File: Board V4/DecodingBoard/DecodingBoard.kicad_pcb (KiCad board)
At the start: 4 copper layers, 47.5 x 41 mm, 71 parts, among them IC1 STM32WBA65CIU6, IC2 RN4871-V_RM140, IC3 MCP111-195I_TO, J1 UJ20-C-H-G-SMT-1-P16-TR, J3 TSM-106-02-T-SH-LC, J4 2053380002, J5 5037630491, J6 5040500691, SW1 TL3305BF100QG, SW2 TL3305BF100QG, U1 ESDS302DBVR, U2 TPS7A7200RGWT, U3 USBLC6-2SC6, U4 TPS2121RUXR

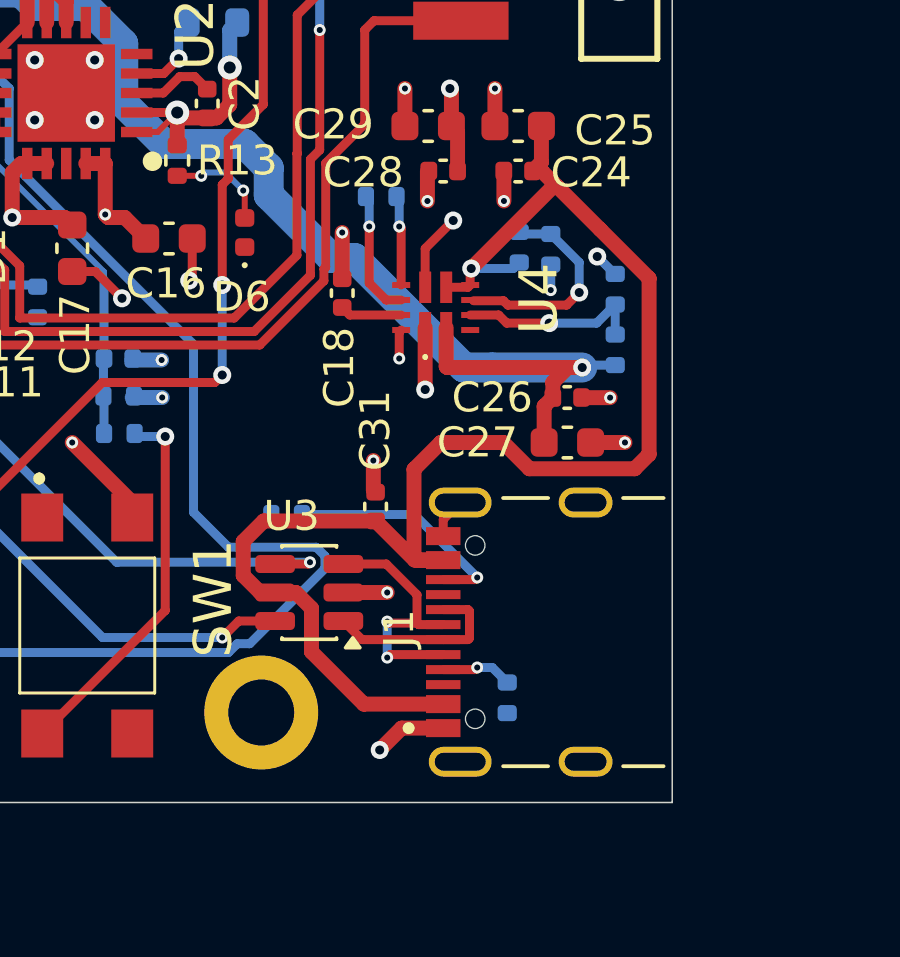
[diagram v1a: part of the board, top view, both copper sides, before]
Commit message: Changed layout for new USB-C connector
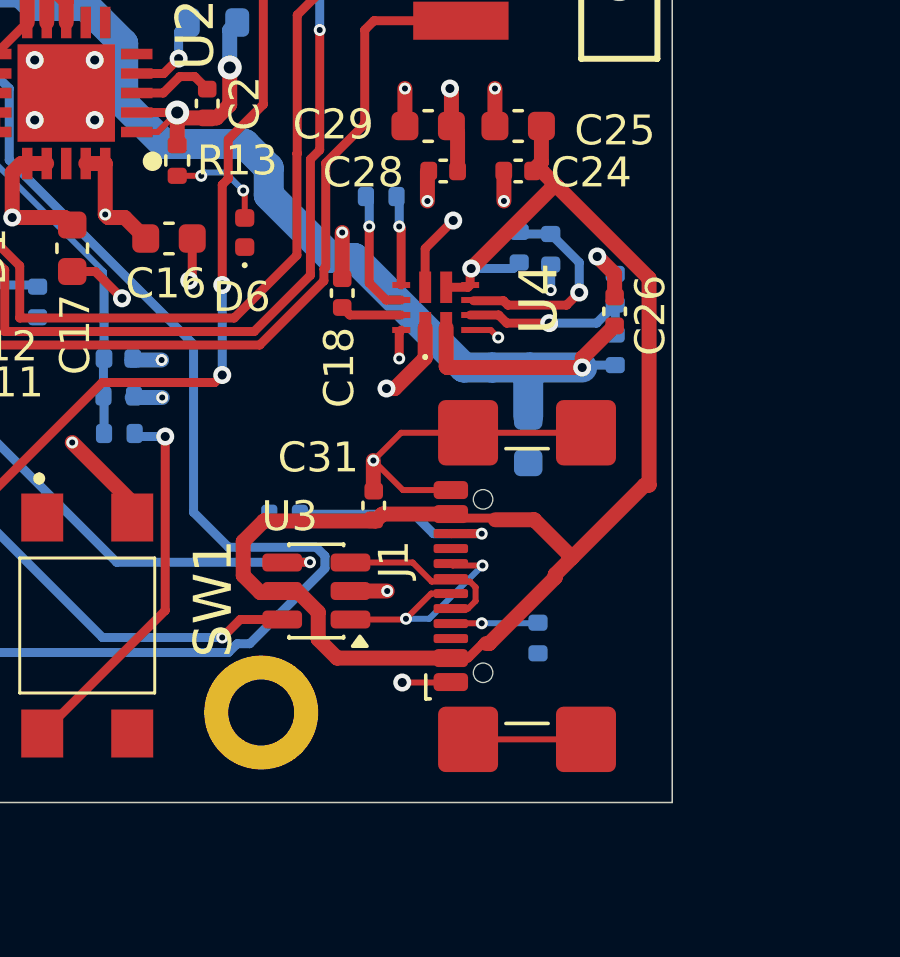
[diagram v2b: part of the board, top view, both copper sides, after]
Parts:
- C27: moved to B.Cu
- J1: value UJ20-C-H-G-SMT-1-P16-TR -> USB_C_Receptacle_USB2.0_16P; footprint Footprints:SAMESKY_UJ20-C-H-G-SMT-1-P16-TR -> Connector_USB:USB_C_Receptacle_GCT_USB4110
- moved J1 3.74 mm to (140.8, 82.8)
- moved C26 3.28 mm to (142.6, 73.6), turned to 90 degrees
- moved R5 2.24 mm to (140.0, 84.5)
- moved C27 1.31 mm to (139.7, 77.9), turned to -90 degrees
- moved U3 0.24 mm to (132.6, 83.0)
- moved C31 0.07 mm to (134.6, 80.1)
- moved R6 0.07 mm to (131.6, 80.4)
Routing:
- net GND: track 81.5 -> 94.6 mm, vias 53 -> 52
- net /USB-C circuit/USB_D-: track 8.84 -> 5.90 mm, vias 2 -> 0
- net /USB-C circuit/USB_D+: track 6.28 -> 8.07 mm, vias 0 -> 2
- net /Power switching and voltage adaptation/from USB-C: track 50.6 -> 52.2 mm
- net +5V: track 22.4 -> 23.0 mm
- net /Power: track 54.8 -> 55.4 mm
- net /USB-C circuit/USB_CC1: track 2.37 -> 2.92 mm
- net /USB-C circuit/USB_CC2: track 7.87 -> 7.36 mm

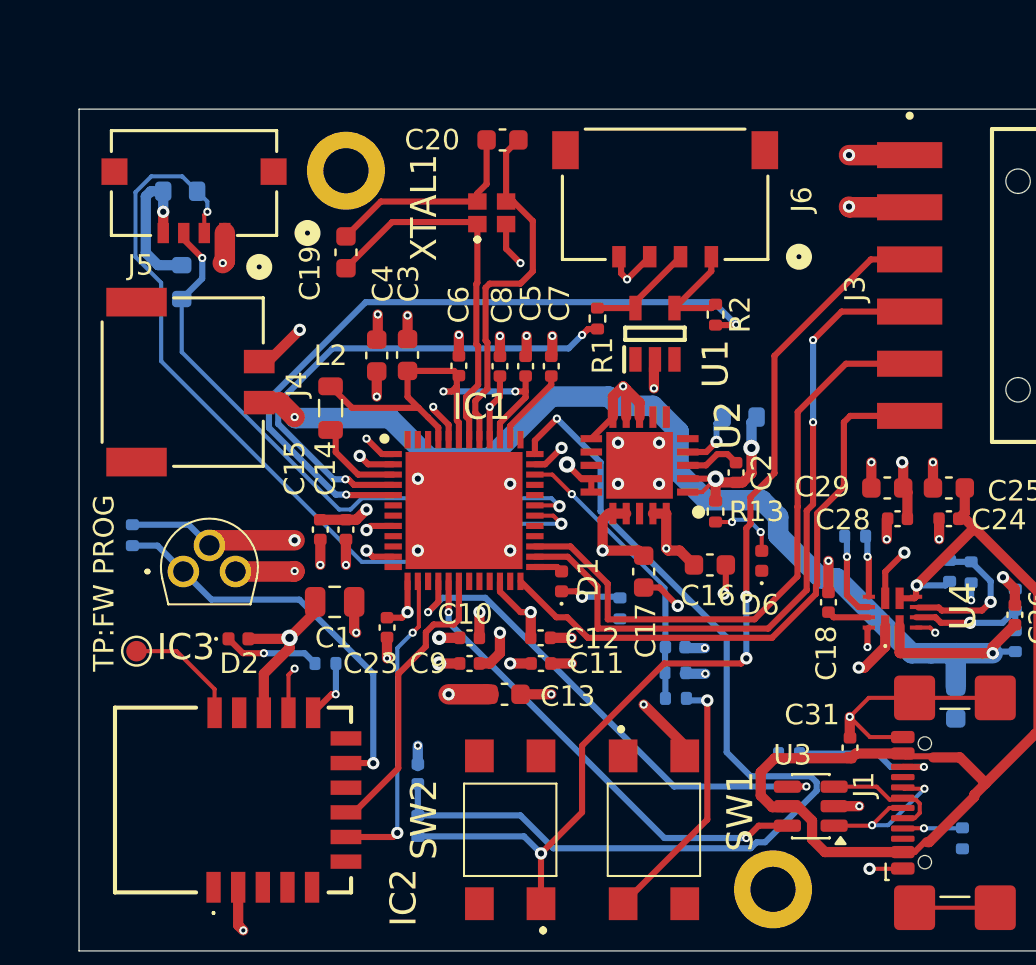
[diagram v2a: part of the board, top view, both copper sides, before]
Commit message: [fix]: reviewed decoding board. Modified J6 connector to 3 pin 1mm pitch Picko-Lock and routed the differential USB
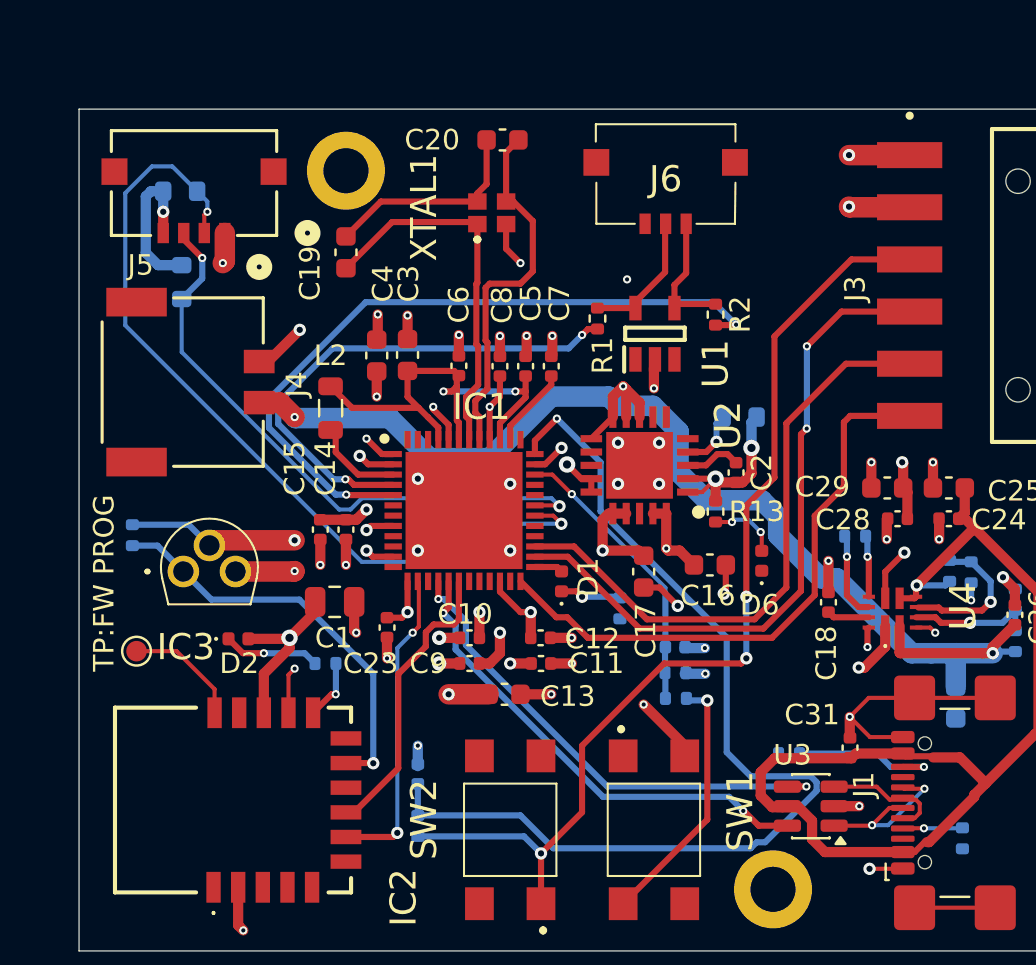
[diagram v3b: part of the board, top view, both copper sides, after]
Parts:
- J6: value 5040500691 -> 5037630391; footprint Footprints:CONN_5040500491_MOL -> Footprints:5037630391
- moved J6 0.74 mm to (125.6, 52.4)
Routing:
- net GND: track 94.6 -> 91.8 mm
- net /SWDCLK: track 34.3 -> 32.9 mm
- net /USART1_TX_CONN: track 5.26 -> 6.56 mm
- net /USART1_RX_CONN: track 5.32 -> 6.43 mm
- net /I2C/I2C_SCL: track 40.4 -> 41.5 mm
- net /SWDIO: track 30.6 -> 29.6 mm
- net /USB-C circuit/D-: track 25.2 -> 24.2 mm
- net /SWD_NRST: track 48.5 -> 49.0 mm

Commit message: [fix:] modified power plane above usb-c routing to have continuous reference.
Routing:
- net GND: track 91.8 -> 92.7 mm, vias 52 -> 53
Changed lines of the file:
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@@
 			)
 		)
-		(property "Datasheet" "https://www.molex.com/en-us/products/part-detail-pdf/5040500691?display=pdf"
+		(property "Datasheet" ""
 			(at 0 0 0)
 			(layer "F.Fab")
@@
 	)
 	(segment
+		(start 130.25 72.35)
+		(end 130.3 72.4)
+		(width 0.2)
+		(layer "F.Cu")
+		(net "GND")
+	)
+	(segment
 		(start 142.58 72.38)
 		(end 142 71.8)
@@
 	)
 	(segment
+		(start 130.25 71.485)
+		(end 130.25 72.35)
+		(width 0.2)
+		(layer "F.Cu")
+		(net "GND")
+	)
+	(segment
 		(start 121 74.75)
 		(end 120 74.75)
@@
 	)
 	(via
+		(at 130.3 72.4)
+		(size 0.6)
+		(drill 0.3)
+		(layers "F.Cu" "B.Cu")
+		(net "GND")
+	)
+	(via
 		(at 125.25 65.25)
 		(size 0.6)
@@
 		(polygon
 			(pts
-				(xy 107 64.5) (xy 103.2 67.6) (xy 100.847344 69.104696) (xy 104.1 76.5) (xy 108.904556 79.083635)
-				(xy 113.654729 82.225845) (xy 128.2 82.8) (xy 129.8 74.8) (xy 122 73.4) (xy 121.936831 72.196155)
-				(xy 120.5 70) (xy 120.224073 66.246138) (xy 121 65.5) (xy 124 68.4) (xy 125 72) (xy 125.4 72.4)
-				(xy 130.895009 71.773382) (xy 133.214453 66.012849) (xy 139 65) (xy 139 88.738462) (xy 138.205589 89.257884)
-				(xy 127.6 89.6) (xy 104.043788 89.359631) (xy 102.939001 88.962238) (xy 98.570677 86.258038) (xy 98.8 64.4)
-				(xy 99.023529 53) (xy 107.893204 53)
+				(xy 106 67.5) (xy 100.9 69.45) (xy 101.25 75.05) (xy 108.904556 79.083635) (xy 112.956747 88.053815)
+				(xy 141.9 83.75) (xy 129.8 74.8) (xy 122 73.4) (xy 121.5 72.25) (xy 119.4 67.2) (xy 121.2 65.2)
+				(xy 122.8 66.4) (xy 125.2 70.2) (xy 125.2 71.4) (xy 130.4 71.4) (xy 133 65) (xy 144.5 64.2) (xy 144 89.55)
+				(xy 138.15 89.55) (xy 127.6 89.6) (xy 103.95 89.55) (xy 102.9 89.49) (xy 97.51 89.5) (xy 97.7 64.55)
+				(xy 97.6 49.45) (xy 112.755745 49.146893)
 			)
 		)
@@
 		(polygon
 			(pts
-				(xy 143.4 64.2) (xy 133 65) (xy 130.4 71.4) (xy 125.2 71.4) (xy 125.2 70.2) (xy 124.2 68.2) (xy 122.8 66.4)
-				(xy 121.2 65.2) (xy 119.4 67.2) (xy 119.5 72) (xy 123.5 75.5) (xy 126.5 75.5) (xy 126 80) (xy 122.4 81.8)
-				(xy 117.4 79.8) (xy 112.325765 79.969141) (xy 106.710982 77.809609) (xy 103.5 75) (xy 101.5 69.5)
-				(xy 106 67.5) (xy 112.755745 49.146893) (xy 126.4 49.8) (xy 131 50.4) (xy 132 50.2) (xy 132.5 50.5)
-				(xy 143 50)
+				(xy 144.5 64.2) (xy 133 65) (xy 130.4 71.4) (xy 125.2 71.4) (xy 125.2 70.2) (xy 124.2 68.2) (xy 122.8 66.4)
+				(xy 121.2 65.2) (xy 119.4 67.2) (xy 120.75 70.8) (xy 122 73.4) (xy 129.8 74.8) (xy 141.9 83.75)
+				(xy 126.25 86.05) (xy 120.4 86.9) (xy 112.956747 88.053815) (xy 108.904556 79.083635) (xy 101.25 75.05)
+				(xy 100.9 69.45) (xy 106 67.5) (xy 112.755745 49.146893) (xy 126.45 49.45) (xy 131.1 49.45) (xy 131.95 49.45)
+				(xy 132.65 49.4) (xy 144.5 49.05)
 			)
 		)

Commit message: [fix:] connected U2 pin 12 to gnd as per datasheet recommendation
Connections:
- U2 pad 12: unconnected-(U2-NC-Pad12) -> GND
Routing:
- net GND: track 92.7 -> 94.4 mm, vias 53 -> 54
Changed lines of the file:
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@@
 			)
 		)
-		(property "Datasheet" ""
+		(property "Datasheet" "https://www.molex.com/en-us/products/part-detail-pdf/5040500691?display=pdf"
 			(at 0 0 0)
 			(layer "F.Fab")
@@
 			(unit
 				(name "A")
-				(pins "SH" "B1" "B12" "A1" "A12" "A9" "B4" "B9" "A4" "A5" "B5" "A7" "B7"
+				(pins "SH" "A1" "A12" "B1" "B12" "A4" "A9" "B4" "B9" "A5" "B5" "A7" "B7"
 					"A6" "B6" "A8" "B8"
 				)
@@
 			(size 0.35 1.05)
 			(layers "F.Cu" "F.Mask" "F.Paste")
-			(net "unconnected-(U2-NC-Pad12)")
+			(net "GND")
 			(pinfunction "NC_12")
-			(pintype "no_connect")
+			(pintype "passive")
 		)
 		(pad "13" smd rect
@@
 	)
 	(segment
+		(start 121.89 64.03)
+		(end 121.89 64.99)
+		(width 0.2)
+		(layer "F.Cu")
+		(net "GND")
+	)
+	(segment
 		(start 138.89 69.95)
 		(end 138.89 68.95)
@@
 	)
 	(segment
+		(start 121.89 64.99)
+		(end 121.95 65.05)
+		(width 0.2)
+		(layer "F.Cu")
+		(net "GND")
+	)
+	(segment
 		(start 128.5 71.2)
 		(end 128.5 72.5)
@@
 	)
 	(segment
+		(start 121.95 65.7)
+		(end 121.95 65.05)
+		(width 0.2)
+		(layer "F.Cu")
+		(net "GND")
+	)
+	(segment
 		(start 124.3 64)
 		(end 124.3 63.3)
@@
 		(net "GND")
 	)
+	(via
+		(at 121.89 64.03)
+		(size 0.6)
+		(drill 0.3)
+		(layers "F.Cu" "B.Cu")
+		(free yes)
+		(net "GND")
+	)
